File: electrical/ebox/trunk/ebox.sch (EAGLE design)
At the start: 162 parts, among them IC1 MAX3221CUE, IC10 SN74LVC1G125, IC11 MAX3221CUE, IC12 INA170, IC13 SN74LVC1G125, IC14 SN74LVC1G125, IC15 MAX3221CUE, IC17 SN74LVC1G125, IC18 SN74LVC1G125, IC19 74ALS04D, IC2 LT3652, IC20 AP1509-33, IC24 AP1509-5, IC3 XMEGA128A1, IC4 LT1161, IC5 SN74LVC1G125, IC6 SN74LVC1G125, IC7 MAX3221CUE, IC8 INA170, IC9 SN74LVC1G125, Q1 FDD4141TO252, U1 BLUETOOTH-RN42, U2 D2523T_, X1 BULLET, X10 DEANS, X11 DEANS, X12 7381-2PG-300, X13 B4B-ZR, X14 BULLET, X17 22-23-2021, X18 7381-3PG-300, X19 7381-3PG-300, X2 BULLET, X20 BULLET, X21 BULLET, X22 BULLET, X23 BULLET, X24 B4B-ZR, X3 17984-7PG-300, X4 BULLET, X5 17984-7PG-300, X6 17984-7PG-300, X7 17984-7PG-300, X8 22-23-2031, X9 22-23-2031

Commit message: Removed switching regulators, replaced with onboard ESC BEC power.
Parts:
- removed C15: 68uF, rcl:CPOL-USD
- removed C22: 220uF, rcl:CPOL-USD
- removed D11, D5: MBRA340T3, diode:MBRA340T3
- removed IC20: AP1509-33, crw:AP1509
- removed IC24: AP1509-5, crw:AP1509
- removed L5, L7: 47uH, crw:L-SRR1280
- removed LED4: RED, led:LEDCHIPLED_1206
- removed R1: 330, rcl:R-US_R0805
- added C1: 68uF, rcl:CPOL-USD
- added IC16: MCP170333MB, linear:MCP170333MB
- added JP1: (no value), jumper:JP2E
- C21: value 68uF -> 1uF; device rcl:CPOL-USD -> rcl:C-USC0805
- C28: value 220uF -> 1uF; device rcl:CPOL-USD -> rcl:C-USC0805
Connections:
- removed net N$40: D5.C, IC20.OUT, L7.1
- removed net N$45: D11.C, IC24.OUT, L5.1
- removed net N$46: LED4.A, R1.1
- new net MOT1_5V: JP1.3, X8-2.S
- new net MOT2_5V: JP1.1, X9-2.S
- net +12V: no longer C15.+, C21.+, IC20.VIN, IC24.VIN
- net +3V3: now also C28.1, IC16.VO; no longer C22.+, IC20.FB, L7.2, R1.2
- net +5V: now also C1.+, C21.1, IC16.VI1, JP1.2; no longer C28.+, IC24.FB, L5.2
- net GND: now also C1.-, C21.2, C28.2, IC16.GND; no longer C15.-, C21.-, C22.-, C28.-, D11.A, D5.A, IC20.GND, IC20.GND1, IC20.GND2, IC20.GND3, IC20.SD, IC24.GND, IC24.GND1, IC24.GND2, IC24.GND3, IC24.SD, LED4.C

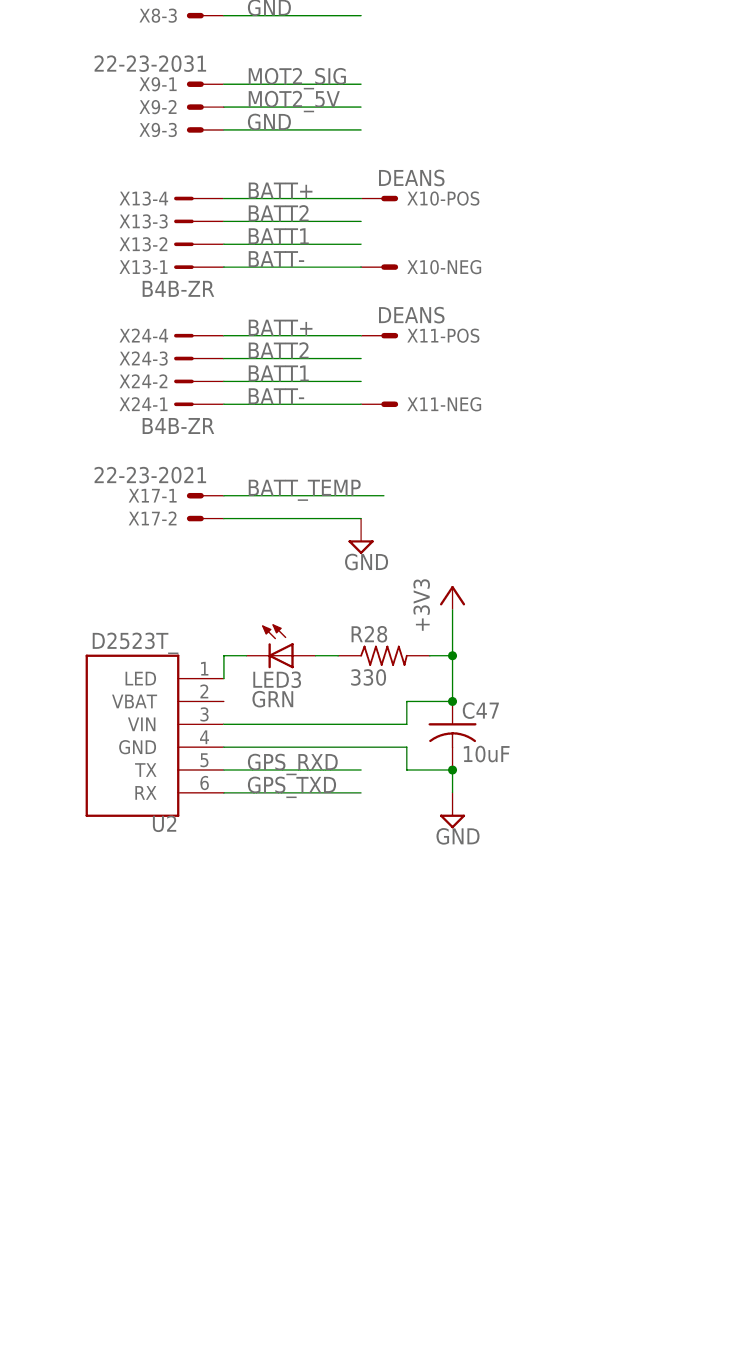
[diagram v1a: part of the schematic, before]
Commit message: Added missing battery connectors for ESC.
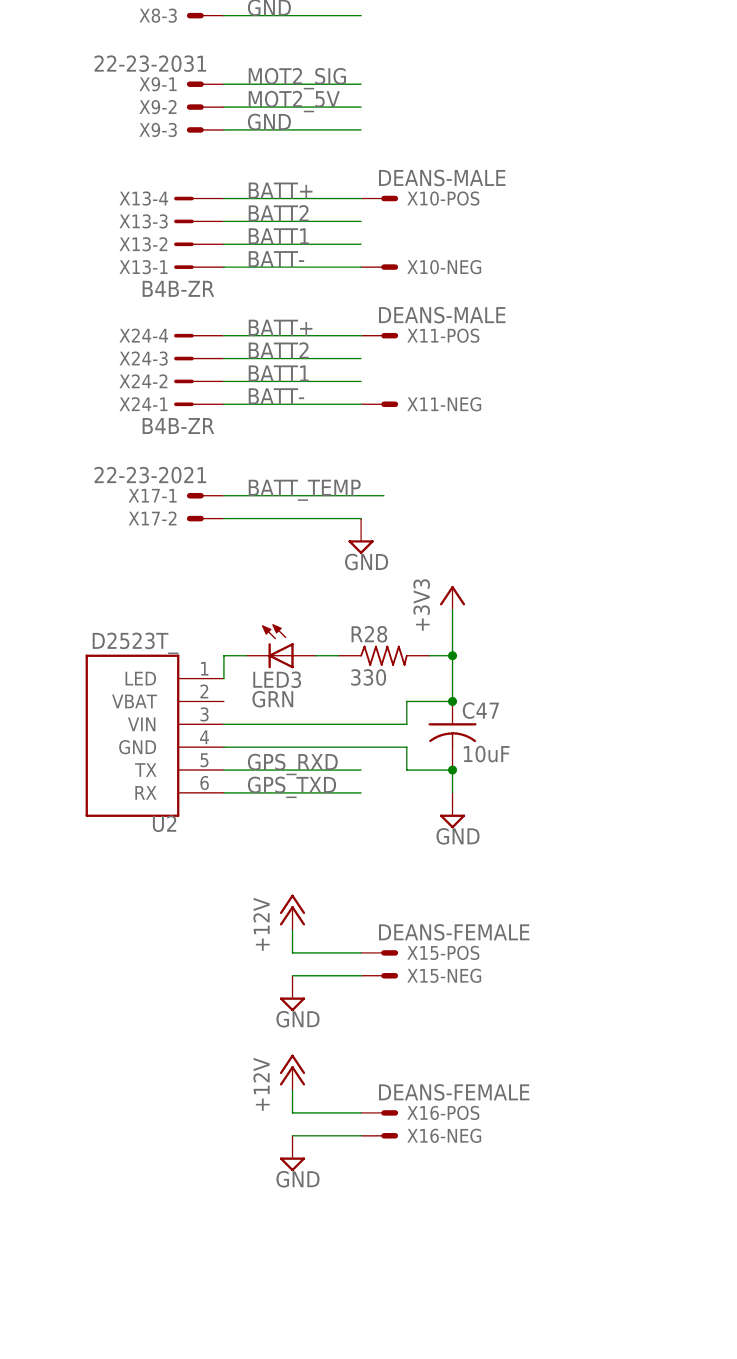
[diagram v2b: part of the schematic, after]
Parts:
- added X15, X16: DEANS-FEMALE, crw:DEANS-FEMALE
- X10, X11: value DEANS -> DEANS-MALE; device crw:DEANS -> crw:DEANS-MALE
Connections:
- net +12V: now also X15-POS.S, X16-POS.S
- net GND: now also X15-NEG.S, X16-NEG.S
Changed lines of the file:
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@@
 <part name="R32" library="rcl" deviceset="R-US_" device="R0805" value="330"/>
 <part name="R33" library="rcl" deviceset="R-US_" device="R0805" value="330"/>
-<part name="X10" library="crw" deviceset="DEANS" device=""/>
-<part name="X11" library="crw" deviceset="DEANS" device=""/>
 <part name="X12" library="crw" deviceset="7381-2PG-300" device=""/>
 <part name="X3" library="crw" deviceset="17984-7PG-300" device=""/>
@@
 <part name="+3V23" library="supply1" deviceset="+3V3" device=""/>
 <part name="IC16" library="linear" deviceset="MCP1703*" device="MB" technology="33"/>
+<part name="X15" library="crw" deviceset="DEANS" device="-FEMALE"/>
+<part name="X16" library="crw" deviceset="DEANS" device="-FEMALE"/>
+<part name="P+1" library="supply1" deviceset="+12V" device=""/>
+<part name="P+8" library="supply1" deviceset="+12V" device=""/>
+<part name="SUPPLY37" library="supply2" deviceset="GND" device=""/>
+<part name="SUPPLY49" library="supply2" deviceset="GND" device=""/>
+<part name="X10" library="crw" deviceset="DEANS" device="-MALE"/>
+<part name="X11" library="crw" deviceset="DEANS" device="-MALE"/>
 </parts>
 <sheets>
@@
 <instance part="R32" gate="G$1" x="345.44" y="134.62" rot="R90"/>
 <instance part="R33" gate="G$1" x="353.06" y="134.62" rot="R90"/>
-<instance part="X10" gate="-POS" x="518.16" y="238.76"/>
-<instance part="X10" gate="-NEG" x="518.16" y="231.14"/>
-<instance part="X11" gate="-POS" x="518.16" y="223.52"/>
-<instance part="X11" gate="-NEG" x="518.16" y="215.9"/>
 <instance part="X12" gate="-1" x="518.16" y="370.84"/>
 <instance part="X12" gate="-2" x="518.16" y="368.3"/>
@@
 <instance part="+3V23" gate="G$1" x="86.36" y="68.58"/>
 <instance part="IC16" gate="G$1" x="71.12" y="63.5"/>
+<instance part="X15" gate="-POS" x="518.16" y="154.94"/>
+<instance part="X15" gate="-NEG" x="518.16" y="152.4"/>
+<instance part="X16" gate="-POS" x="518.16" y="137.16"/>
+<instance part="X16" gate="-NEG" x="518.16" y="134.62"/>
+<instance part="P+1" gate="1" x="508" y="160.02"/>
+<instance part="P+8" gate="1" x="508" y="142.24"/>
+<instance part="SUPPLY37" gate="GND" x="508" y="149.86"/>
+<instance part="SUPPLY49" gate="GND" x="508" y="132.08"/>
+<instance part="X10" gate="-POS" x="518.16" y="238.76"/>
+<instance part="X10" gate="-NEG" x="518.16" y="231.14"/>
+<instance part="X11" gate="-POS" x="518.16" y="223.52"/>
+<instance part="X11" gate="-NEG" x="518.16" y="215.9"/>
 </instances>
 <busses>
@@
 <pinref part="IC16" gate="G$1" pin="GND"/>
 </segment>
+<segment>
+<pinref part="SUPPLY37" gate="GND" pin="GND"/>
+<pinref part="X15" gate="-NEG" pin="S"/>
+<wire x1="508" y1="152.4" x2="515.62" y2="152.4" width="0.1524" layer="91"/>
+</segment>
+<segment>
+<pinref part="SUPPLY49" gate="GND" pin="GND"/>
+<pinref part="X16" gate="-NEG" pin="S"/>
+<wire x1="508" y1="134.62" x2="515.62" y2="134.62" width="0.1524" layer="91"/>
+</segment>
 </net>
 <net name="S1_12V" class="0">
@@
 <junction x="447.04" y="406.4"/>
 </segment>
-</net>
+<segment>
+<pinref part="P+1" gate="1" pin="+12V"/>
+<wire x1="508" y1="157.48" x2="508" y2="154.94" width="0.1524" layer="91"/>
+<pinref part="X15" gate="-POS" pin="S"/>
+<wire x1="508" y1="154.94" x2="515.62" y2="154.94" width="0.1524" layer="91"/>
+</segment>
+<segment>
+<pinref part="P+8" gate="1" pin="+12V"/>
+<wire x1="508" y1="139.7" x2="508" y2="137.16" width="0.1524" layer="91"/>
+<pinref part="X16" gate="-POS" pin="S"/>
+<wire x1="508" y1="137.16" x2="515.62" y2="137.16" width="0.1524" layer="91"/>
+</segment>
+</net>

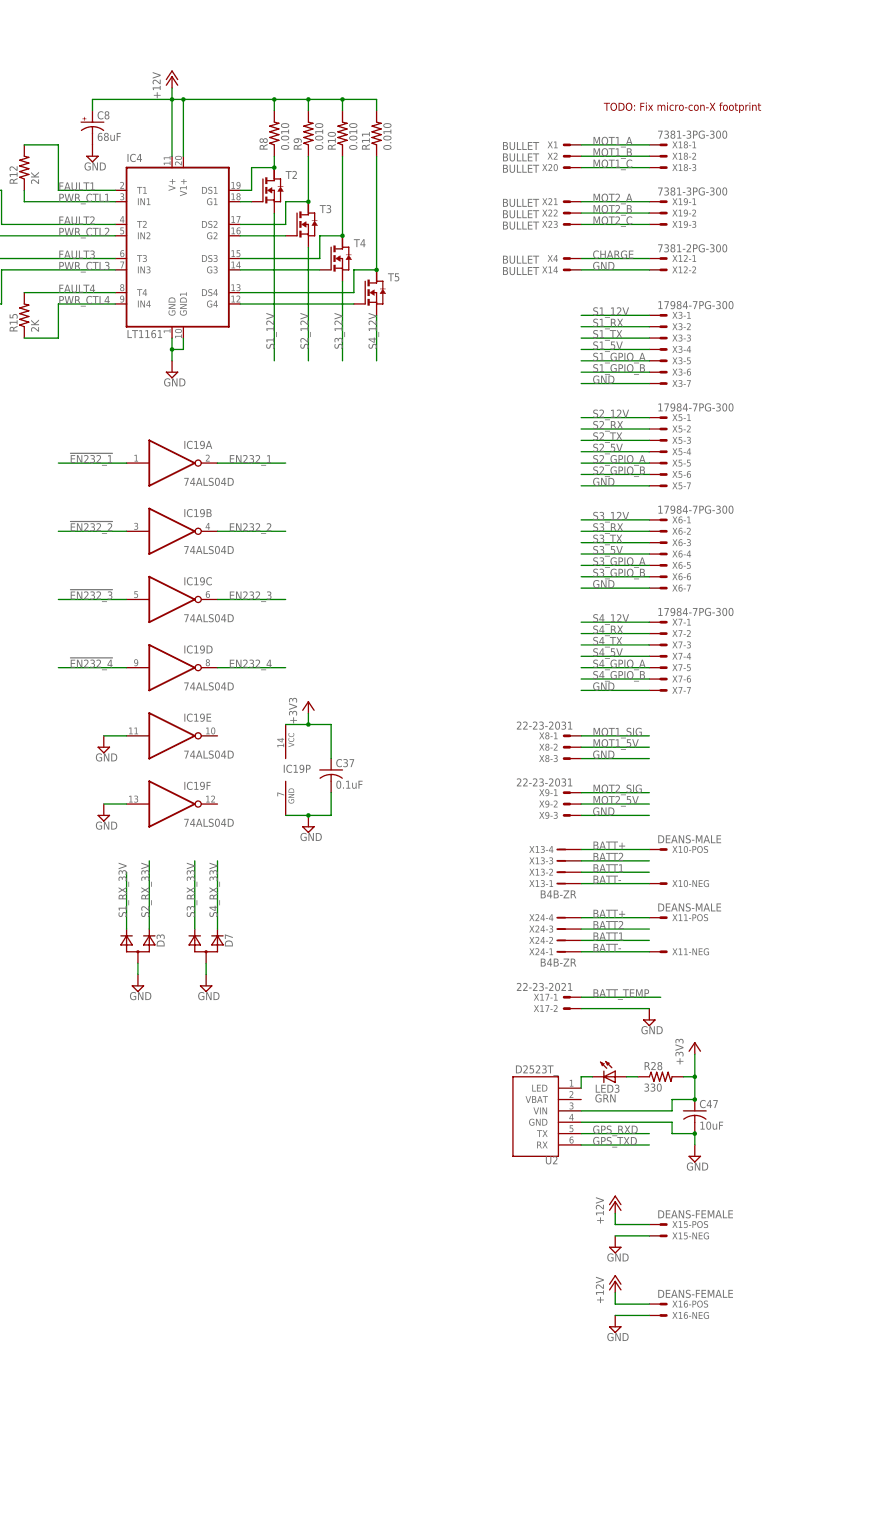
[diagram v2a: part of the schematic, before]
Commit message: Added USB connector, swapped FETs for smaller form factor.
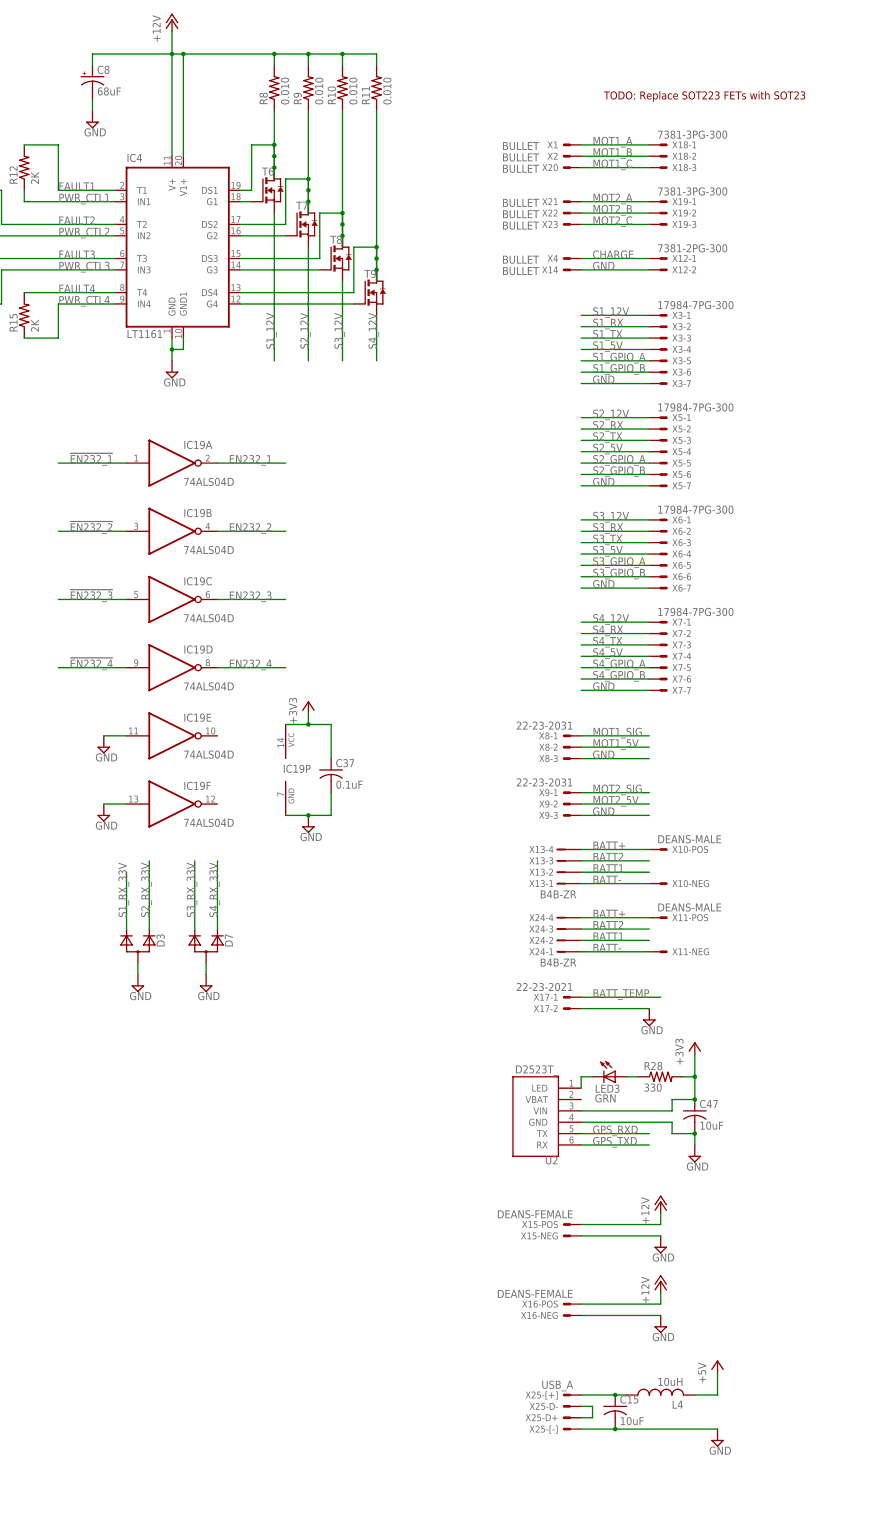
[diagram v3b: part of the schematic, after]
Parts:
- removed T2, T3, T4, T5: (no value), zetex:NMOSSOT223
- added C15: 10uF, rcl:C-USC0805
- added L4: 10uH, rcl:L-USL2012C
- added T6, T7, T8, T9: (no value), zetex:NMOSSOT23-6
- added X25: USB_A, crw:USB_A
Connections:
- new net N$40: C15.1, L4.1, X25-[+].S
- new net N$45: X25-D+.S, X25-D-.S
- net +5V: now also L4.2
- net GND: now also C15.2, X25-[-].S
- net N$12: now also T6.D, T6.D1, T6.D2, T6.D3; no longer T2.D
- net N$14: now also T7.D, T7.D1, T7.D2, T7.D3; no longer T3.D
- net N$15: now also T8.D, T8.D1, T8.D2, T8.D3; no longer T4.D
- net N$16: now also T9.D, T9.D1, T9.D2, T9.D3; no longer T5.D
- net N$17: now also T6.G; no longer T2.G
- net N$18: now also T7.G; no longer T3.G
- net N$19: now also T8.G; no longer T4.G
- net N$20: now also T9.G; no longer T5.G
- net S1_12V: now also T6.S; no longer T2.S
- net S2_12V: now also T7.S; no longer T3.S
- net S3_12V: now also T8.S; no longer T4.S
- net S4_12V: now also T9.S; no longer T5.S
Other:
- note added: "TODO: Replace SOT223 FETs with SOT23"
- note removed: "TODO: Fix micro-con-X footprint"
- moved on the sheet: C8, R10, R11, R8, R9, X15-NEG, X15-POS, X16-NEG, X16-POS

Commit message: Generally figured out better layout for connectors, renamed some stuff for clarity.
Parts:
- removed X18, X19: 7381-3PG-300, crw:7381-3PG-300
- removed X24: B4B-ZR, con-jst:B4B-ZR
- removed X25: USB_A, crw:USB_A
- added B1, B2, B7, B8: BULLET, crw:BULLET
- X1, X2: value BULLET -> 7381-3PG-300; device crw:BULLET -> crw:7381-3PG-300
- X11: value DEANS-MALE -> B4B-ZR; device crw:DEANS-MALE -> con-jst:B4B-ZR
- X12: value 7381-2PG-300 -> DEANS-MALE; device crw:7381-2PG-300 -> crw:DEANS-MALE
- X14: value BULLET -> 22-23-2021; device crw:BULLET -> con-molex:22-23-2021
- X17: value 22-23-2021 -> USB_A; device con-molex:22-23-2021 -> crw:USB_A
- X3: value 17984-7PG-300 -> 7381-2PG-300; device crw:17984-7PG-300 -> crw:7381-2PG-300
- X4: value BULLET -> 17984-7PG-300; device crw:BULLET -> crw:17984-7PG-300
- renumbered X20 to B3, X21 to B4, X22 to B5, X23 to B6
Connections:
- net BATT+: now also X11-4.1, X12-POS.S; no longer X11-POS.S, X24-4.1
- net BATT-: now also X11-1.1, X12-NEG.S; no longer X11-NEG.S, X24-1.1
- net BATT1: now also X11-2.1; no longer X24-2.1
- net BATT2: now also X11-3.1; no longer X24-3.1
- net BATT_TEMP: now also X14-1.S; no longer X17-1.S
- net CHARGE: now also B7.S, X3-1.S; no longer X12-1.S, X4.S
- net GND: now also B8.S, X14-2.S, X17-[-].S, X3-2.S, X4-7.S; no longer X12-2.S, X14.S, X17-2.S, X25-[-].S, X3-7.S
- net MOT1_A: now also B1.S, X1-1.S; no longer X1.S, X18-1.S
- net MOT1_B: now also B2.S, X1-2.S; no longer X18-2.S, X2.S
- net MOT1_C: now also X1-3.S; no longer X18-3.S
- net MOT2_A: now also X2-1.S; no longer X19-1.S
- net MOT2_B: now also X2-2.S; no longer X19-2.S
- net MOT2_C: now also X2-3.S; no longer X19-3.S
- net N$40: now also X17-[+].S; no longer X25-[+].S
- net N$45: now also X17-D+.S, X17-D-.S; no longer X25-D+.S, X25-D-.S
- net S1_12V: now also X4-1.S; no longer X3-1.S
- net S1_5V: now also X4-4.S; no longer X3-4.S
- net S1_GPIO_A: now also X4-5.S; no longer X3-5.S
- net S1_GPIO_B: now also X4-6.S; no longer X3-6.S
- net S1_RX: now also X4-2.S; no longer X3-2.S
- net S1_TX: now also X4-3.S; no longer X3-3.S
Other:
- moved on the sheet: X1-1, X13-1, X13-2, X13-3, X13-4, X14-1, X2-1, X3-1, X3-2, X4-1
